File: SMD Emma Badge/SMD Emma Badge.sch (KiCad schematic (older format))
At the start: 1 part, among them J1 Conn_01x02_Male

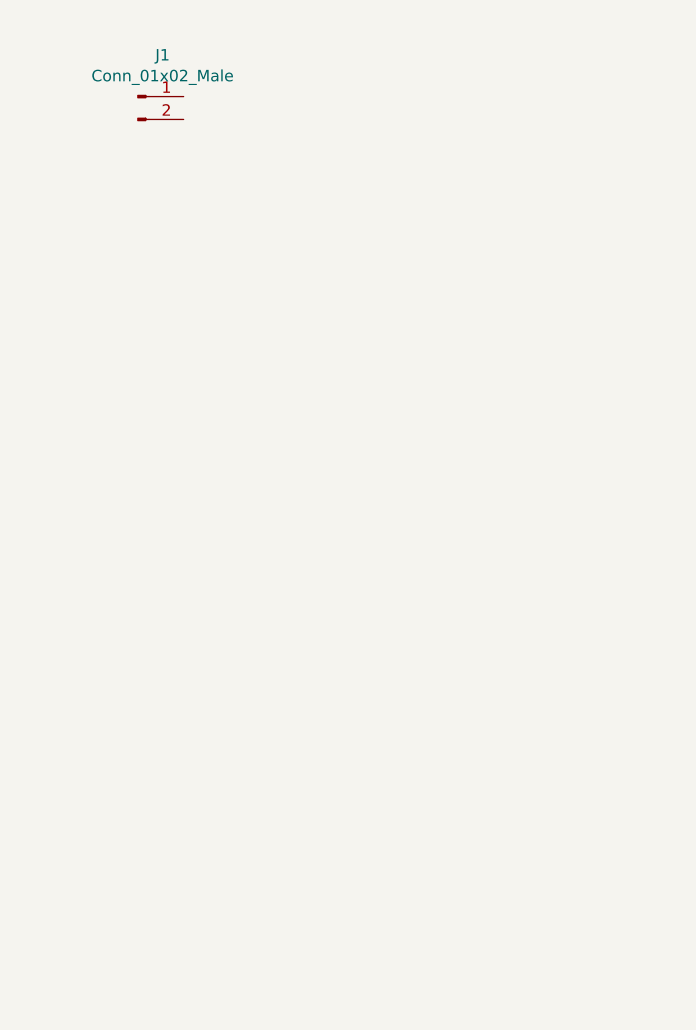
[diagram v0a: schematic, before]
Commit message: Adding in clocks
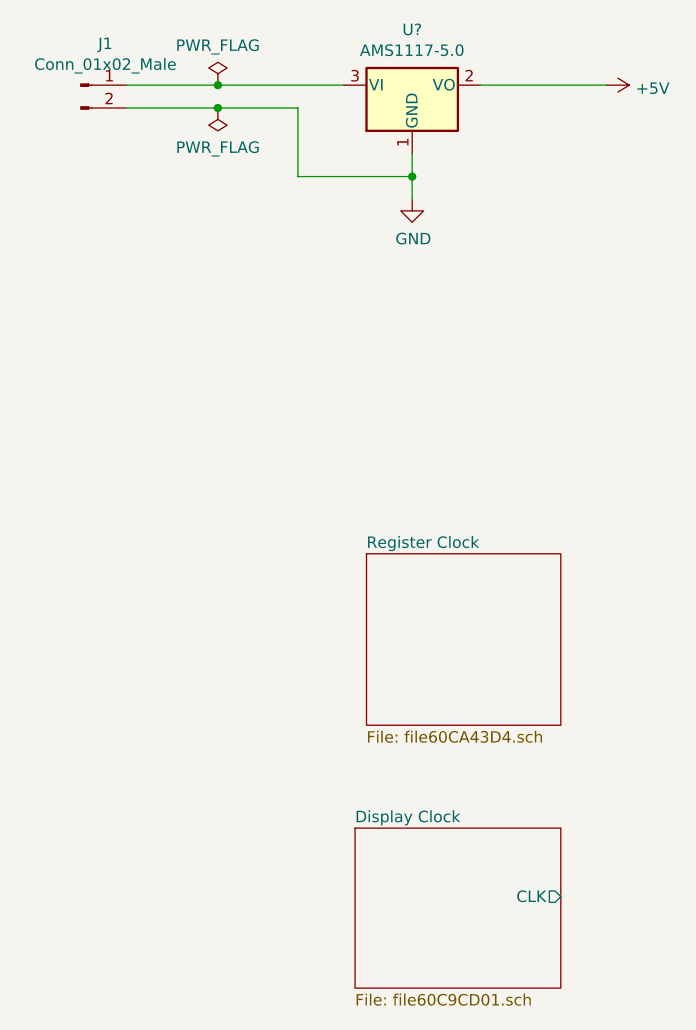
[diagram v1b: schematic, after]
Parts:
- added U?: AMS1117-5.0, Package_TO_SOT_SMD:SOT-223-3_TabPin2, symbol Regulator_Linear:AMS1117-5.0
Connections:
- net at J1.1 (Pin_1): now also U?.3 (VI)
- net GND: now reaches J1.2 (Pin_2)
- net GND: now also U?.1 (GND)
- new net +5V: U?.2 (VO)
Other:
- moved on the sheet: J1
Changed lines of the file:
@@
 $Descr A4 11693 8268
 encoding utf-8
-Sheet 1 1
+Sheet 1 3
 Title ""
 Date ""
@@
 L Connector:Conn_01x02_Male J1
 U 1 1 60C994E1
-P 1350 1550
-F 0 "J1" H 1458 1731 50  0000 C CNN
-F 1 "Conn_01x02_Male" H 1458 1640 50  0000 C CNN
-F 2 "Connector_PinHeader_2.54mm:PinHeader_1x02_P2.54mm_Vertical" H 1350 1550 50  0001 C CNN
-F 3 "~" H 1350 1550 50  0001 C CNN
-	1    1350 1550
+P 1100 1500
+F 0 "J1" H 1208 1681 50  0000 C CNN
+F 1 "Conn_01x02_Male" H 1208 1590 50  0000 C CNN
+F 2 "Connector_PinHeader_2.54mm:PinHeader_1x02_P2.54mm_Vertical" H 1100 1500 50  0001 C CNN
+F 3 "~" H 1100 1500 50  0001 C CNN
+	1    1100 1500
 	1    0    0    -1
 $EndComp
+$Comp
+L Regulator_Linear:AMS1117-5.0 U?
+U 1 1 60C9A1C8
+P 2550 1500
+F 0 "U?" H 2550 1742 50  0000 C CNN
+F 1 "AMS1117-5.0" H 2550 1651 50  0000 C CNN
+F 2 "Package_TO_SOT_SMD:SOT-223-3_TabPin2" H 2550 1700 50  0001 C CNN
+F 3 "http://www.advanced-monolithic.com/pdf/ds1117.pdf" H 2650 1250 50  0001 C CNN
+F 4 "C6187" H 2550 1500 50  0001 C CNN "LCSC"
+	1    2550 1500
+	1    0    0    -1
+$EndComp
+Wire Wire Line
+	1300 1500 1700 1500
+$Comp
+L power:GND #PWR?
+U 1 1 60C9BE86
+P 2550 2000
+F 0 "#PWR?" H 2550 1750 50  0001 C CNN
+F 1 "GND" H 2555 1827 50  0000 C CNN
+F 2 "" H 2550 2000 50  0001 C CNN
+F 3 "" H 2550 2000 50  0001 C CNN
+	1    2550 2000
+	1    0    0    -1
+$EndComp
+Wire Wire Line
+	2550 1800 2550 1900
+Wire Wire Line
+	1300 1600 1700 1600
+Wire Wire Line
+	2050 1600 2050 1900
+Wire Wire Line
+	2050 1900 2550 1900
+Connection ~ 2550 1900
+Wire Wire Line
+	2550 1900 2550 2000
+$Comp
+L power:PWR_FLAG #FLG?
+U 1 1 60C951D2
+P 1700 1500
+F 0 "#FLG?" H 1700 1575 50  0001 C CNN
+F 1 "PWR_FLAG" H 1700 1673 50  0000 C CNN
+F 2 "" H 1700 1500 50  0001 C CNN
+F 3 "~" H 1700 1500 50  0001 C CNN
+	1    1700 1500
+	1    0    0    -1
+$EndComp
+Connection ~ 1700 1500
+Wire Wire Line
+	1700 1500 2250 1500
+$Comp
+L power:PWR_FLAG #FLG?
+U 1 1 60C957A4
+P 1700 1600
+F 0 "#FLG?" H 1700 1675 50  0001 C CNN
+F 1 "PWR_FLAG" H 1700 1773 50  0000 C CNN
+F 2 "" H 1700 1600 50  0001 C CNN
+F 3 "~" H 1700 1600 50  0001 C CNN
+	1    1700 1600
+	-1   0    0    1
+$EndComp
+Connection ~ 1700 1600
+Wire Wire Line
+	1700 1600 2050 1600
+$Comp
+L power:+5V #PWR?
+U 1 1 60C95FD9
+P 3400 1500
+F 0 "#PWR?" H 3400 1350 50  0001 C CNN
+F 1 "+5V" V 3415 1628 50  0000 L CNN
+F 2 "" H 3400 1500 50  0001 C CNN
+F 3 "" H 3400 1500 50  0001 C CNN
+	1    3400 1500
+	0    1    1    0
+$EndComp
+Wire Wire Line
+	2850 1500 3400 1500
+$Sheet
+S 2300 4750 900  700
+U 60C9CD02
+F0 "Display Clock" 50
+F1 "file60C9CD01.sch" 50
+F2 "CLK" O R 3200 5050 50
+$EndSheet
+$Sheet
+S 2350 3550 850  750
+U 60CA43D5
+F0 "Register Clock" 50
+F1 "file60CA43D4.sch" 50
+$EndSheet
 $EndSCHEMATC

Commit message: Working through basics of the LFSR
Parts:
- gave numbers to parts that had none: 1
- renumbered J1 to J101
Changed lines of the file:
@@
 $Descr A4 11693 8268
 encoding utf-8
-Sheet 1 3
+Sheet 1 4
 Title ""
 Date ""
@@
 $EndDescr
 $Comp
-L Connector:Conn_01x02_Male J1
+L Connector:Conn_01x02_Male J101
 U 1 1 60C994E1
 P 1100 1500
-F 0 "J1" H 1208 1681 50  0000 C CNN
+F 0 "J101" H 1208 1681 50  0000 C CNN
 F 1 "Conn_01x02_Male" H 1208 1590 50  0000 C CNN
 F 2 "Connector_PinHeader_2.54mm:PinHeader_1x02_P2.54mm_Vertical" H 1100 1500 50  0001 C CNN
@@
 $EndComp
 $Comp
-L Regulator_Linear:AMS1117-5.0 U?
+L Regulator_Linear:AMS1117-5.0 U101
 U 1 1 60C9A1C8
 P 2550 1500
-F 0 "U?" H 2550 1742 50  0000 C CNN
+F 0 "U101" H 2550 1742 50  0000 C CNN
 F 1 "AMS1117-5.0" H 2550 1651 50  0000 C CNN
 F 2 "Package_TO_SOT_SMD:SOT-223-3_TabPin2" H 2550 1700 50  0001 C CNN
@@
 	1300 1500 1700 1500
 $Comp
-L power:GND #PWR?
+L power:GND #PWR0101
 U 1 1 60C9BE86
 P 2550 2000
-F 0 "#PWR?" H 2550 1750 50  0001 C CNN
+F 0 "#PWR0101" H 2550 1750 50  0001 C CNN
 F 1 "GND" H 2555 1827 50  0000 C CNN
 F 2 "" H 2550 2000 50  0001 C CNN
@@
 	2550 1900 2550 2000
 $Comp
-L power:PWR_FLAG #FLG?
+L power:PWR_FLAG #FLG0101
 U 1 1 60C951D2
 P 1700 1500
-F 0 "#FLG?" H 1700 1575 50  0001 C CNN
+F 0 "#FLG0101" H 1700 1575 50  0001 C CNN
 F 1 "PWR_FLAG" H 1700 1673 50  0000 C CNN
 F 2 "" H 1700 1500 50  0001 C CNN
@@
 	1700 1500 2250 1500
 $Comp
-L power:PWR_FLAG #FLG?
+L power:PWR_FLAG #FLG0102
 U 1 1 60C957A4
 P 1700 1600
-F 0 "#FLG?" H 1700 1675 50  0001 C CNN
+F 0 "#FLG0102" H 1700 1675 50  0001 C CNN
 F 1 "PWR_FLAG" H 1700 1773 50  0000 C CNN
 F 2 "" H 1700 1600 50  0001 C CNN
@@
 	1700 1600 2050 1600
 $Comp
-L power:+5V #PWR?
+L power:+5V #PWR0102
 U 1 1 60C95FD9
 P 3400 1500
-F 0 "#PWR?" H 3400 1350 50  0001 C CNN
+F 0 "#PWR0102" H 3400 1350 50  0001 C CNN
 F 1 "+5V" V 3415 1628 50  0000 L CNN
 F 2 "" H 3400 1500 50  0001 C CNN
@@
 F0 "Register Clock" 50
 F1 "file60CA43D4.sch" 50
+F2 "CLK" O R 3200 3900 50
 $EndSheet
+$Sheet
+S 4500 3700 1750 1800
+U 60CB0F52
+F0 "LFSR" 50
+F1 "file60CB0F51.sch" 50
+F2 "REGCLK" I L 4500 3900 50
+F3 "DISPCLK" I L 4500 5050 50
+F4 "DISPE" O R 6250 4150 50
+F5 "DISPM1" O R 6250 4350 50
+F6 "DISPM2" O R 6250 4500 50
+F7 "DISPA" O R 6250 4650 50
+$EndSheet
+Wire Wire Line
+	3200 5050 4500 5050
+Wire Wire Line
+	3200 3900 4500 3900
 $EndSCHEMATC

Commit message: Working on letters
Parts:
- added H101, H102: MountingHole, MountingHole:MountingHole_2.5mm, symbol Mechanical:MountingHole
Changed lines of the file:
@@
 $Descr A4 11693 8268
 encoding utf-8
-Sheet 1 4
+Sheet 1 8
 Title ""
 Date ""
@@
 	1300 1500 1700 1500
 $Comp
-L power:GND #PWR0101
+L power:GND #PWR0102
 U 1 1 60C9BE86
 P 2550 2000
-F 0 "#PWR0101" H 2550 1750 50  0001 C CNN
+F 0 "#PWR0102" H 2550 1750 50  0001 C CNN
 F 1 "GND" H 2555 1827 50  0000 C CNN
 F 2 "" H 2550 2000 50  0001 C CNN
@@
 	1700 1600 2050 1600
 $Comp
-L power:+5V #PWR0102
+L power:+5V #PWR0101
 U 1 1 60C95FD9
 P 3400 1500
-F 0 "#PWR0102" H 3400 1350 50  0001 C CNN
+F 0 "#PWR0101" H 3400 1350 50  0001 C CNN
 F 1 "+5V" V 3415 1628 50  0000 L CNN
 F 2 "" H 3400 1500 50  0001 C CNN
@@
 Wire Wire Line
 	3200 3900 4500 3900
+$Sheet
+S 7450 2400 600  600
+U 60CD2CFA
+F0 "LED-E" 50
+F1 "file60CD2CF9.sch" 50
+F2 "LED-E" I L 7450 2700 50
+$EndSheet
+Wire Wire Line
+	6250 4150 6700 4150
+Wire Wire Line
+	6700 4150 6700 2700
+Wire Wire Line
+	6700 2700 7450 2700
+$Sheet
+S 7450 3600 700  700
+U 60D27A84
+F0 "LED-M1" 50
+F1 "file60D27A83.sch" 50
+F2 "LED-M1" I L 7450 3950 50
+$EndSheet
+Wire Wire Line
+	6250 4350 7000 4350
+Wire Wire Line
+	7000 4350 7000 3950
+Wire Wire Line
+	7000 3950 7450 3950
+$Sheet
+S 7500 4650 650  600
+U 60D72CD2
+F0 "LED-M2" 50
+F1 "file60D72CD1.sch" 50
+F2 "LED-M2" I L 7500 4900 50
+$EndSheet
+Wire Wire Line
+	6250 4500 7000 4500
+Wire Wire Line
+	7000 4500 7000 4900
+Wire Wire Line
+	7000 4900 7500 4900
+$Sheet
+S 7500 5450 650  700
+U 60DC2975
+F0 "LED-A" 50
+F1 "file60DC2974.sch" 50
+F2 "LED-A" I L 7500 5850 50
+$EndSheet
+Wire Wire Line
+	6250 4650 6700 4650
+Wire Wire Line
+	6700 4650 6700 5850
+Wire Wire Line
+	6700 5850 7500 5850
+$Comp
+L Mechanical:MountingHole H101
+U 1 1 60E181EE
+P 950 2700
+F 0 "H101" H 1050 2746 50  0000 L CNN
+F 1 "MountingHole" H 1050 2655 50  0000 L CNN
+F 2 "MountingHole:MountingHole_2.5mm" H 950 2700 50  0001 C CNN
+F 3 "~" H 950 2700 50  0001 C CNN
+	1    950  2700
+	1    0    0    -1
+$EndComp
+$Comp
+L Mechanical:MountingHole H102
+U 1 1 60E188DE
+P 1750 2700
+F 0 "H102" H 1850 2746 50  0000 L CNN
+F 1 "MountingHole" H 1850 2655 50  0000 L CNN
+F 2 "MountingHole:MountingHole_2.5mm" H 1750 2700 50  0001 C CNN
+F 3 "~" H 1750 2700 50  0001 C CNN
+	1    1750 2700
+	1    0    0    -1
+$EndComp
 $EndSCHEMATC
